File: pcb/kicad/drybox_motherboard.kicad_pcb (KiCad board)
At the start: 2 copper layers, 100 x 100 mm, 11 parts

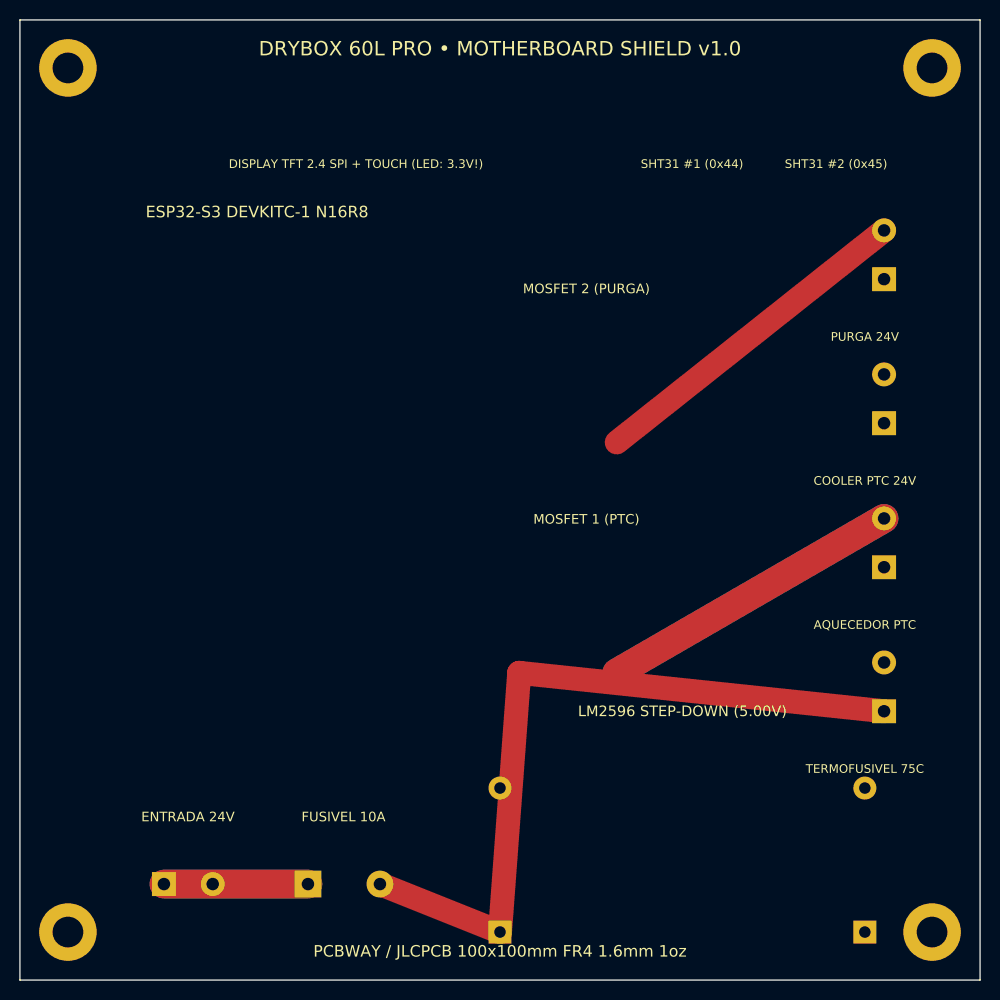
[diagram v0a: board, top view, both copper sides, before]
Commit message: feat(pcb): adiciona serigrafia vetorial completa com nomes e pinagens de todos os componentes na placa
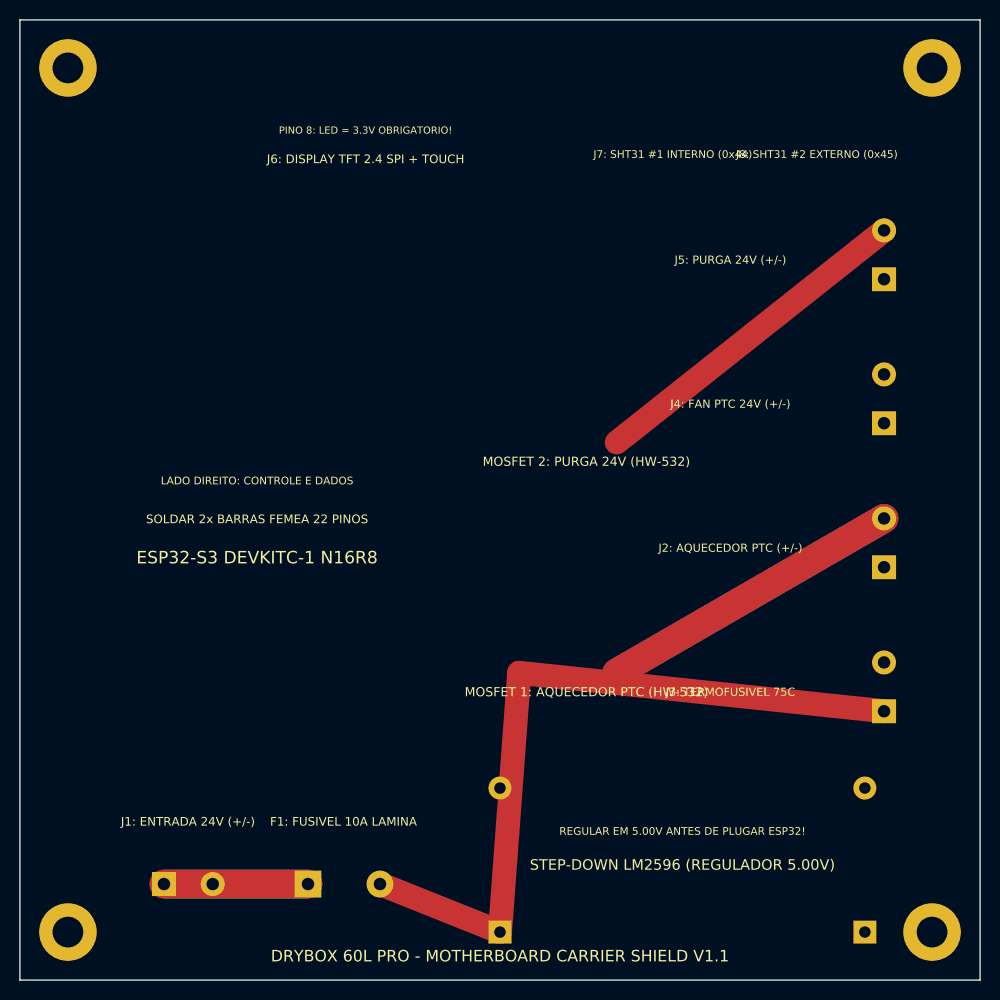
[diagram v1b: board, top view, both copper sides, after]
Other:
- board text added: "DRYBOX 60L PRO - MOTHERBOARD CARRIER SHIELD V1.1"
- board text added: "F1: FUSIVEL 10A LAMINA"
- board text added: "J1: ENTRADA 24V (+/-)"
- board text added: "J2: AQUECEDOR PTC (+/-)"
- board text added: "J3: TERMOFUSIVEL 75C"
- board text added: "J4: FAN PTC 24V (+/-)"
- board text added: "J5: PURGA 24V (+/-)"
- board text added: "J6: DISPLAY TFT 2.4 SPI + TOUCH"
- board text added: "J7: SHT31 #1 INTERNO (0x44)"
- board text added: "J8: SHT31 #2 EXTERNO (0x45)"
- board text added: "LADO DIREITO: CONTROLE E DADOS"
- board text added: "MOSFET 1: AQUECEDOR PTC (HW-532)"
- board text added: "MOSFET 2: PURGA 24V (HW-532)"
- board text added: "PINO 8: LED = 3.3V OBRIGATORIO!"
- board text added: "REGULAR EM 5.00V ANTES DE PLUGAR ESP32!"
- board text added: "SOLDAR 2x BARRAS FEMEA 22 PINOS"
- board text added: "STEP-DOWN LM2596 (REGULADOR 5.00V)"
- board text removed: "AQUECEDOR PTC"
- board text removed: "COOLER PTC 24V"
- board text removed: "DISPLAY TFT 2.4 SPI + TOUCH (LED: 3.3V!)"
- board text removed: "DRYBOX 60L PRO • MOTHERBOARD SHIELD v1.0"
- board text removed: "ENTRADA 24V"
- board text removed: "FUSIVEL 10A"
- board text removed: "LM2596 STEP-DOWN (5.00V)"
- board text removed: "MOSFET 1 (PTC)"
- board text removed: "MOSFET 2 (PURGA)"
- board text removed: "PCBWAY / JLCPCB 100x100mm FR4 1.6mm 1oz"
- board text removed: "PURGA 24V"
- board text removed: "SHT31 #1 (0x44)"
- board text removed: "SHT31 #2 (0x45)"
- board text removed: "TERMOFUSIVEL 75C"
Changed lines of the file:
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@@
   (gr_rect (start 0 0) (end 100 100) (layer "Edge.Cuts") (width 0.15) (fill none))
   ;; Textos de Serigrafia
-  (gr_text "DRYBOX 60L PRO • MOTHERBOARD SHIELD v1.0" (at 50 3) (layer "F.SilkS")
-    (effects (font (size 1.5 1.5) (thickness 0.25)))
-  )
-  (gr_text "PCBWAY / JLCPCB 100x100mm FR4 1.6mm 1oz" (at 50 97) (layer "F.SilkS")
-    (effects (font (size 1.2 1.2) (thickness 0.2)))
-  )
-  (gr_text "ENTRADA 24V" (at 17.5 83) (layer "F.SilkS") (effects (font (size 1.0 1.0) (thickness 0.2))))
-  (gr_text "FUSIVEL 10A" (at 33.7 83) (layer "F.SilkS") (effects (font (size 1.0 1.0) (thickness 0.2))))
-  (gr_text "LM2596 STEP-DOWN (5.00V)" (at 69 72) (layer "F.SilkS") (effects (font (size 1.1 1.1) (thickness 0.2))))
-  (gr_text "ESP32-S3 DEVKITC-1 N16R8" (at 24.7 20) (layer "F.SilkS") (effects (font (size 1.2 1.2) (thickness 0.2))))
-  (gr_text "MOSFET 1 (PTC)" (at 59 52) (layer "F.SilkS") (effects (font (size 1.0 1.0) (thickness 0.2))))
-  (gr_text "MOSFET 2 (PURGA)" (at 59 28) (layer "F.SilkS") (effects (font (size 1.0 1.0) (thickness 0.2))))
-  (gr_text "TERMOFUSIVEL 75C" (at 88 78) (layer "F.SilkS") (effects (font (size 0.9 0.9) (thickness 0.18))))
-  (gr_text "AQUECEDOR PTC" (at 88 63) (layer "F.SilkS") (effects (font (size 0.9 0.9) (thickness 0.18))))
-  (gr_text "COOLER PTC 24V" (at 88 48) (layer "F.SilkS") (effects (font (size 0.9 0.9) (thickness 0.18))))
-  (gr_text "PURGA 24V" (at 88 33) (layer "F.SilkS") (effects (font (size 0.9 0.9) (thickness 0.18))))
-  (gr_text "DISPLAY TFT 2.4 SPI + TOUCH (LED: 3.3V!)" (at 35 15) (layer "F.SilkS") (effects (font (size 0.9 0.9) (thickness 0.18))))
-  (gr_text "SHT31 #1 (0x44)" (at 70 15) (layer "F.SilkS") (effects (font (size 0.9 0.9) (thickness 0.18))))
-  (gr_text "SHT31 #2 (0x45)" (at 85 15) (layer "F.SilkS") (effects (font (size 0.9 0.9) (thickness 0.18))))
-  ;; Furos de Fixacao M3
+  ;; Textos de Serigrafia Detalhados
+  (gr_text "DRYBOX 60L PRO - MOTHERBOARD CARRIER SHIELD V1.1" (at 50 97.5) (layer "F.SilkS") (effects (font (size 1.2 1.2) (thickness 0.18))))
+  (gr_text "J1: ENTRADA 24V (+/-)" (at 17.5 83.5) (layer "F.SilkS") (effects (font (size 0.9 0.9) (thickness 0.18))))
+  (gr_text "F1: FUSIVEL 10A LAMINA" (at 33.7 83.5) (layer "F.SilkS") (effects (font (size 0.9 0.9) (thickness 0.18))))
+  (gr_text "STEP-DOWN LM2596 (REGULADOR 5.00V)" (at 69 88) (layer "F.SilkS") (effects (font (size 1.1 1.1) (thickness 0.18))))
+  (gr_text "REGULAR EM 5.00V ANTES DE PLUGAR ESP32!" (at 69 84.5) (layer "F.SilkS") (effects (font (size 0.8 0.8) (thickness 0.18))))
+  (gr_text "ESP32-S3 DEVKITC-1 N16R8" (at 24.7 56) (layer "F.SilkS") (effects (font (size 1.3 1.3) (thickness 0.18))))
+  (gr_text "SOLDAR 2x BARRAS FEMEA 22 PINOS" (at 24.7 52) (layer "F.SilkS") (effects (font (size 0.9 0.9) (thickness 0.18))))
+  (gr_text "LADO DIREITO: CONTROLE E DADOS" (at 24.7 48) (layer "F.SilkS") (effects (font (size 0.8 0.8) (thickness 0.18))))
+  (gr_text "MOSFET 1: AQUECEDOR PTC (HW-532)" (at 59 70) (layer "F.SilkS") (effects (font (size 0.95 0.95) (thickness 0.18))))
+  (gr_text "MOSFET 2: PURGA 24V (HW-532)" (at 59 46) (layer "F.SilkS") (effects (font (size 0.95 0.95) (thickness 0.18))))
+  (gr_text "J3: TERMOFUSIVEL 75C" (at 74 70) (layer "F.SilkS") (effects (font (size 0.85 0.85) (thickness 0.18))))
+  (gr_text "J2: AQUECEDOR PTC (+/-)" (at 74 55) (layer "F.SilkS") (effects (font (size 0.85 0.85) (thickness 0.18))))
+  (gr_text "J4: FAN PTC 24V (+/-)" (at 74 40) (layer "F.SilkS") (effects (font (size 0.85 0.85) (thickness 0.18))))
+  (gr_text "J5: PURGA 24V (+/-)" (at 74 25) (layer "F.SilkS") (effects (font (size 0.85 0.85) (thickness 0.18))))
+  (gr_text "J6: DISPLAY TFT 2.4 SPI + TOUCH" (at 36 14.5) (layer "F.SilkS") (effects (font (size 0.9 0.9) (thickness 0.18))))
+  (gr_text "PINO 8: LED = 3.3V OBRIGATORIO!" (at 36 11.5) (layer "F.SilkS") (effects (font (size 0.75 0.75) (thickness 0.18))))
+  (gr_text "J7: SHT31 #1 INTERNO (0x44)" (at 68 14) (layer "F.SilkS") (effects (font (size 0.8 0.8) (thickness 0.18))))
+  (gr_text "J8: SHT31 #2 EXTERNO (0x45)" (at 83 14) (layer "F.SilkS") (effects (font (size 0.8 0.8) (thickness 0.18))))
   (footprint "MountingHole:MountingHole_3.2mm_M3_Pad" (layer "F.Cu") (at 5 5)
     (pad "1" thru_hole circle (at 0 0) (size 6.0 6.0) (drill 3.2) (layers *.Cu *.Mask) (net 3 "GND"))

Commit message: fix(pcb): corrige posicionamento da serigrafia do ESP32 e afasta titulo dos furos M3
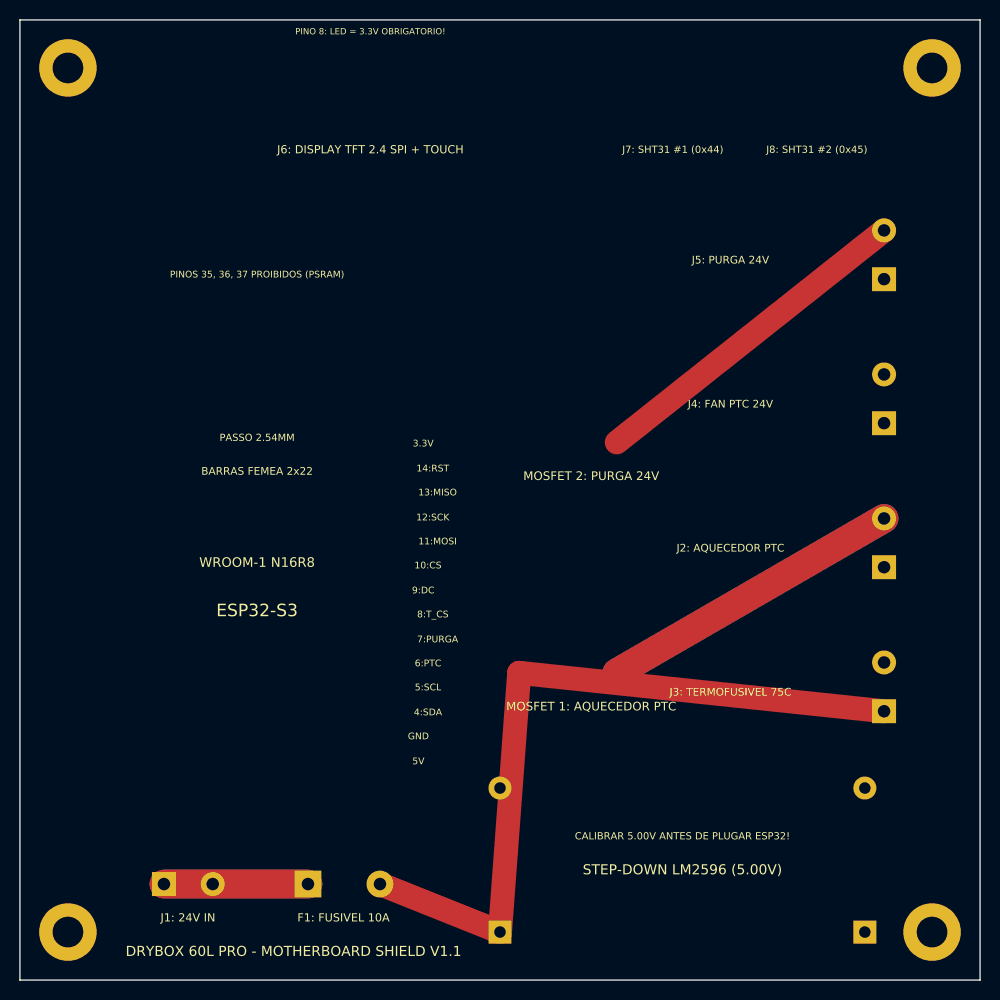
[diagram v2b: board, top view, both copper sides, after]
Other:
- board text added: "10:CS"
- board text added: "11:MOSI"
- board text added: "12:SCK"
- board text added: "13:MISO"
- board text added: "14:RST"
- board text added: "3.3V"
- board text added: "4:SDA"
- board text added: "5:SCL"
- board text added: "5V"
- board text added: "6:PTC"
- board text added: "7:PURGA"
- board text added: "8:T_CS"
- board text added: "9:DC"
- board text added: "BARRAS FEMEA 2x22"
- board text added: "CALIBRAR 5.00V ANTES DE PLUGAR ESP32!"
- board text added: "DRYBOX 60L PRO - MOTHERBOARD SHIELD V1.1"
- board text added: "ESP32-S3"
- board text added: "F1: FUSIVEL 10A"
- board text added: "GND"
- board text added: "J1: 24V IN"
- board text added: "J2: AQUECEDOR PTC"
- board text added: "J4: FAN PTC 24V"
- board text added: "J5: PURGA 24V"
- board text added: "J7: SHT31 #1 (0x44)"
- board text added: "J8: SHT31 #2 (0x45)"
- board text added: "MOSFET 1: AQUECEDOR PTC"
- board text added: "MOSFET 2: PURGA 24V"
- board text added: "PASSO 2.54MM"
- board text added: "PINOS 35, 36, 37 PROIBIDOS (PSRAM)"
- board text added: "STEP-DOWN LM2596 (5.00V)"
- board text added: "WROOM-1 N16R8"
- board text removed: "DRYBOX 60L PRO - MOTHERBOARD CARRIER SHIELD V1.1"
- board text removed: "ESP32-S3 DEVKITC-1 N16R8"
- board text removed: "F1: FUSIVEL 10A LAMINA"
- board text removed: "J1: ENTRADA 24V (+/-)"
- board text removed: "J2: AQUECEDOR PTC (+/-)"
- board text removed: "J4: FAN PTC 24V (+/-)"
- board text removed: "J5: PURGA 24V (+/-)"
- board text removed: "J7: SHT31 #1 INTERNO (0x44)"
- board text removed: "J8: SHT31 #2 EXTERNO (0x45)"
- board text removed: "LADO DIREITO: CONTROLE E DADOS"
- board text removed: "MOSFET 1: AQUECEDOR PTC (HW-532)"
- board text removed: "MOSFET 2: PURGA 24V (HW-532)"
- board text removed: "REGULAR EM 5.00V ANTES DE PLUGAR ESP32!"
- board text removed: "SOLDAR 2x BARRAS FEMEA 22 PINOS"
- board text removed: "STEP-DOWN LM2596 (REGULADOR 5.00V)"
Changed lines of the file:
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@@
   ;; Textos de Serigrafia
   ;; Textos de Serigrafia Detalhados
-  (gr_text "DRYBOX 60L PRO - MOTHERBOARD CARRIER SHIELD V1.1" (at 50 97.5) (layer "F.SilkS") (effects (font (size 1.2 1.2) (thickness 0.18))))
-  (gr_text "J1: ENTRADA 24V (+/-)" (at 17.5 83.5) (layer "F.SilkS") (effects (font (size 0.9 0.9) (thickness 0.18))))
-  (gr_text "F1: FUSIVEL 10A LAMINA" (at 33.7 83.5) (layer "F.SilkS") (effects (font (size 0.9 0.9) (thickness 0.18))))
-  (gr_text "STEP-DOWN LM2596 (REGULADOR 5.00V)" (at 69 88) (layer "F.SilkS") (effects (font (size 1.1 1.1) (thickness 0.18))))
-  (gr_text "REGULAR EM 5.00V ANTES DE PLUGAR ESP32!" (at 69 84.5) (layer "F.SilkS") (effects (font (size 0.8 0.8) (thickness 0.18))))
-  (gr_text "ESP32-S3 DEVKITC-1 N16R8" (at 24.7 56) (layer "F.SilkS") (effects (font (size 1.3 1.3) (thickness 0.18))))
-  (gr_text "SOLDAR 2x BARRAS FEMEA 22 PINOS" (at 24.7 52) (layer "F.SilkS") (effects (font (size 0.9 0.9) (thickness 0.18))))
-  (gr_text "LADO DIREITO: CONTROLE E DADOS" (at 24.7 48) (layer "F.SilkS") (effects (font (size 0.8 0.8) (thickness 0.18))))
-  (gr_text "MOSFET 1: AQUECEDOR PTC (HW-532)" (at 59 70) (layer "F.SilkS") (effects (font (size 0.95 0.95) (thickness 0.18))))
-  (gr_text "MOSFET 2: PURGA 24V (HW-532)" (at 59 46) (layer "F.SilkS") (effects (font (size 0.95 0.95) (thickness 0.18))))
-  (gr_text "J3: TERMOFUSIVEL 75C" (at 74 70) (layer "F.SilkS") (effects (font (size 0.85 0.85) (thickness 0.18))))
-  (gr_text "J2: AQUECEDOR PTC (+/-)" (at 74 55) (layer "F.SilkS") (effects (font (size 0.85 0.85) (thickness 0.18))))
-  (gr_text "J4: FAN PTC 24V (+/-)" (at 74 40) (layer "F.SilkS") (effects (font (size 0.85 0.85) (thickness 0.18))))
-  (gr_text "J5: PURGA 24V (+/-)" (at 74 25) (layer "F.SilkS") (effects (font (size 0.85 0.85) (thickness 0.18))))
-  (gr_text "J6: DISPLAY TFT 2.4 SPI + TOUCH" (at 36 14.5) (layer "F.SilkS") (effects (font (size 0.9 0.9) (thickness 0.18))))
-  (gr_text "PINO 8: LED = 3.3V OBRIGATORIO!" (at 36 11.5) (layer "F.SilkS") (effects (font (size 0.75 0.75) (thickness 0.18))))
-  (gr_text "J7: SHT31 #1 INTERNO (0x44)" (at 68 14) (layer "F.SilkS") (effects (font (size 0.8 0.8) (thickness 0.18))))
-  (gr_text "J8: SHT31 #2 EXTERNO (0x45)" (at 83 14) (layer "F.SilkS") (effects (font (size 0.8 0.8) (thickness 0.18))))
+  ;; Textos de Serigrafia Corrigidos
+  (gr_text "DRYBOX 60L PRO - MOTHERBOARD SHIELD V1.1" (at 28.5 97) (layer "F.SilkS") (effects (font (size 1.05 1.05) (thickness 0.18))))
+  (gr_text "J1: 24V IN" (at 17.5 93.5) (layer "F.SilkS") (effects (font (size 0.85 0.85) (thickness 0.18))))
+  (gr_text "F1: FUSIVEL 10A" (at 33.7 93.5) (layer "F.SilkS") (effects (font (size 0.85 0.85) (thickness 0.18))))
+  (gr_text "STEP-DOWN LM2596 (5.00V)" (at 69 88.5) (layer "F.SilkS") (effects (font (size 1.05 1.05) (thickness 0.18))))
+  (gr_text "CALIBRAR 5.00V ANTES DE PLUGAR ESP32!" (at 69 85) (layer "F.SilkS") (effects (font (size 0.75 0.75) (thickness 0.18))))
+  (gr_text "ESP32-S3" (at 24.7 61.5) (layer "F.SilkS") (effects (font (size 1.3 1.3) (thickness 0.18))))
+  (gr_text "WROOM-1 N16R8" (at 24.7 56.5) (layer "F.SilkS") (effects (font (size 1 1) (thickness 0.18))))
+  (gr_text "BARRAS FEMEA 2x22" (at 24.7 47) (layer "F.SilkS") (effects (font (size 0.8 0.8) (thickness 0.18))))
+  (gr_text "PASSO 2.54MM" (at 24.7 43.5) (layer "F.SilkS") (effects (font (size 0.75 0.75) (thickness 0.18))))
+  (gr_text "5V" (at 41.5 77.2) (layer "F.SilkS") (effects (font (size 0.7 0.7) (thickness 0.18))))
+  (gr_text "GND" (at 41.5 74.6) (layer "F.SilkS") (effects (font (size 0.7 0.7) (thickness 0.18))))
+  (gr_text "4:SDA" (at 42.5 72.1) (layer "F.SilkS") (effects (font (size 0.7 0.7) (thickness 0.18))))
+  (gr_text "5:SCL" (at 42.5 69.5) (layer "F.SilkS") (effects (font (size 0.7 0.7) (thickness 0.18))))
+  (gr_text "6:PTC" (at 42.5 67) (layer "F.SilkS") (effects (font (size 0.7 0.7) (thickness 0.18))))
+  (gr_text "7:PURGA" (at 43.5 64.5) (layer "F.SilkS") (effects (font (size 0.7 0.7) (thickness 0.18))))
+  (gr_text "8:T_CS" (at 43 61.9) (layer "F.SilkS") (effects (font (size 0.7 0.7) (thickness 0.18))))
+  (gr_text "9:DC" (at 42 59.4) (layer "F.SilkS") (effects (font (size 0.7 0.7) (thickness 0.18))))
+  (gr_text "10:CS" (at 42.5 56.8) (layer "F.SilkS") (effects (font (size 0.7 0.7) (thickness 0.18))))
+  (gr_text "11:MOSI" (at 43.5 54.3) (layer "F.SilkS") (effects (font (size 0.7 0.7) (thickness 0.18))))
+  (gr_text "12:SCK" (at 43 51.8) (layer "F.SilkS") (effects (font (size 0.7 0.7) (thickness 0.18))))
+  (gr_text "13:MISO" (at 43.5 49.2) (layer "F.SilkS") (effects (font (size 0.7 0.7) (thickness 0.18))))
+  (gr_text "14:RST" (at 43 46.7) (layer "F.SilkS") (effects (font (size 0.7 0.7) (thickness 0.18))))
+  (gr_text "3.3V" (at 42 44.1) (layer "F.SilkS") (effects (font (size 0.7 0.7) (thickness 0.18))))
+  (gr_text "PINOS 35, 36, 37 PROIBIDOS (PSRAM)" (at 24.7 26.5) (layer "F.SilkS") (effects (font (size 0.7 0.7) (thickness 0.18))))
+  (gr_text "MOSFET 1: AQUECEDOR PTC" (at 59.5 71.5) (layer "F.SilkS") (effects (font (size 0.9 0.9) (thickness 0.18))))
+  (gr_text "MOSFET 2: PURGA 24V" (at 59.5 47.5) (layer "F.SilkS") (effects (font (size 0.9 0.9) (thickness 0.18))))
+  (gr_text "J3: TERMOFUSIVEL 75C" (at 74 70) (layer "F.SilkS") (effects (font (size 0.8 0.8) (thickness 0.18))))
+  (gr_text "J2: AQUECEDOR PTC" (at 74 55) (layer "F.SilkS") (effects (font (size 0.8 0.8) (thickness 0.18))))
+  (gr_text "J4: FAN PTC 24V" (at 74 40) (layer "F.SilkS") (effects (font (size 0.8 0.8) (thickness 0.18))))
+  (gr_text "J5: PURGA 24V" (at 74 25) (layer "F.SilkS") (effects (font (size 0.8 0.8) (thickness 0.18))))
+  (gr_text "J6: DISPLAY TFT 2.4 SPI + TOUCH" (at 36.5 13.5) (layer "F.SilkS") (effects (font (size 0.85 0.85) (thickness 0.18))))
+  (gr_text "PINO 8: LED = 3.3V OBRIGATORIO!" (at 36.5 1.2) (layer "F.SilkS") (effects (font (size 0.65 0.65) (thickness 0.18))))
+  (gr_text "J7: SHT31 #1 (0x44)" (at 68 13.5) (layer "F.SilkS") (effects (font (size 0.75 0.75) (thickness 0.18))))
+  (gr_text "J8: SHT31 #2 (0x45)" (at 83 13.5) (layer "F.SilkS") (effects (font (size 0.75 0.75) (thickness 0.18))))
   (footprint "MountingHole:MountingHole_3.2mm_M3_Pad" (layer "F.Cu") (at 5 5)
     (pad "1" thru_hole circle (at 0 0) (size 6.0 6.0) (drill 3.2) (layers *.Cu *.Mask) (net 3 "GND"))
